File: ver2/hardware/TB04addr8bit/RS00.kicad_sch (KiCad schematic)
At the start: 34 parts, among them IC201 74HC161N, IC202 74HC161N, IC203 74HC161N, IC204 74HC161N, U201 74LS253, U202 74LS253, U203 74LS253, U204 74LS253

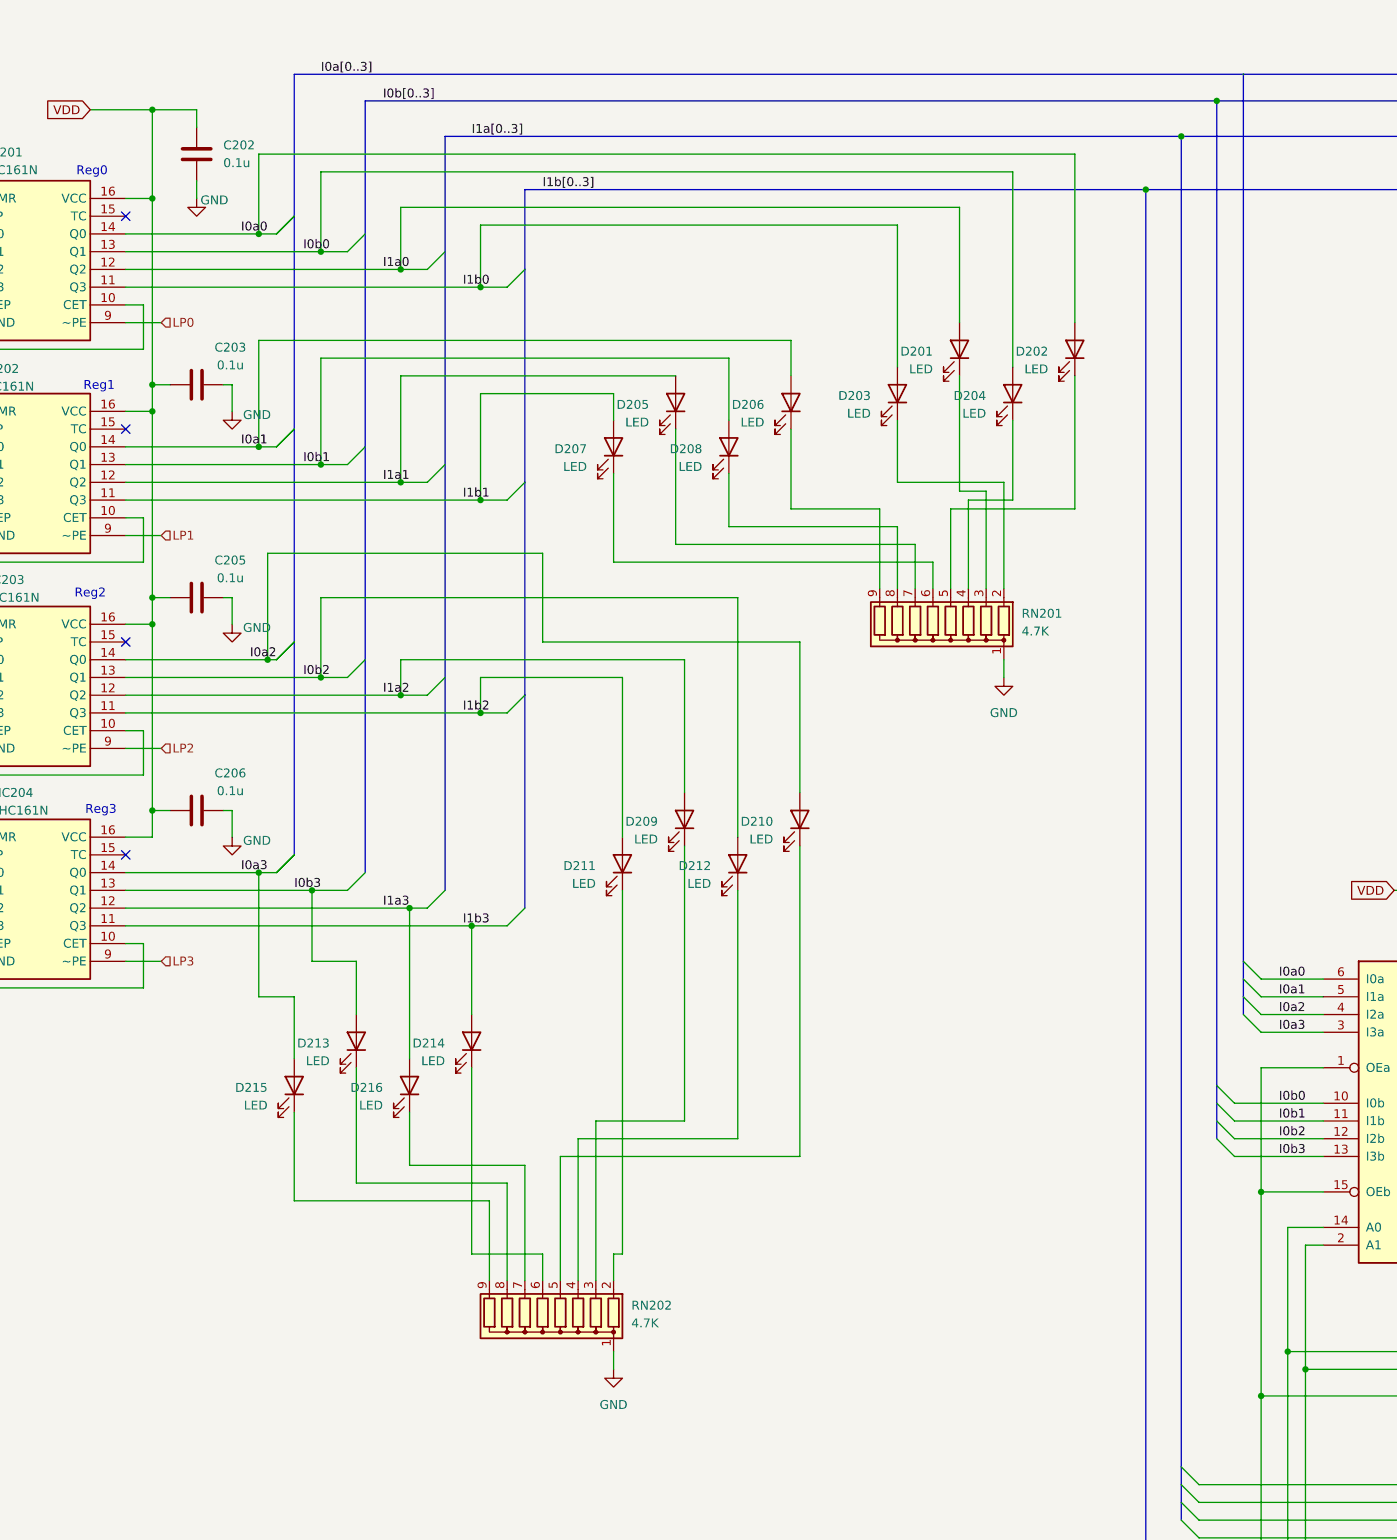
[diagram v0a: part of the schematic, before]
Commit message: ver2: 表示器を2x5コネクタ方式に変更し外付け7segIFで見せる構成に
本体のレジスタLED等を廃止し、7segIF互換の2x5コネクタ21個で外に出す方式へ。
InterFaceシートを新設しOPC/OPR0-11・MD・PC_Qを追加、R0-7とalu_codeも
コネクタ化。SP0-2のLEDを追加。既存部品のネット変更は0件で巻き添えなし。

あわせて命令ROM(U604)にバンク切替スイッチSW601(SW_Coded_SH-7050)を追加し、
A8-A11で256バイト×16バンクを選べるようにした。

要対応: A8-A11にプルダウン(10K)が無く、未選択の接点が開放で浮く。

Co-Authored-By: Claude Opus 5 <noreply@anthropic.com>
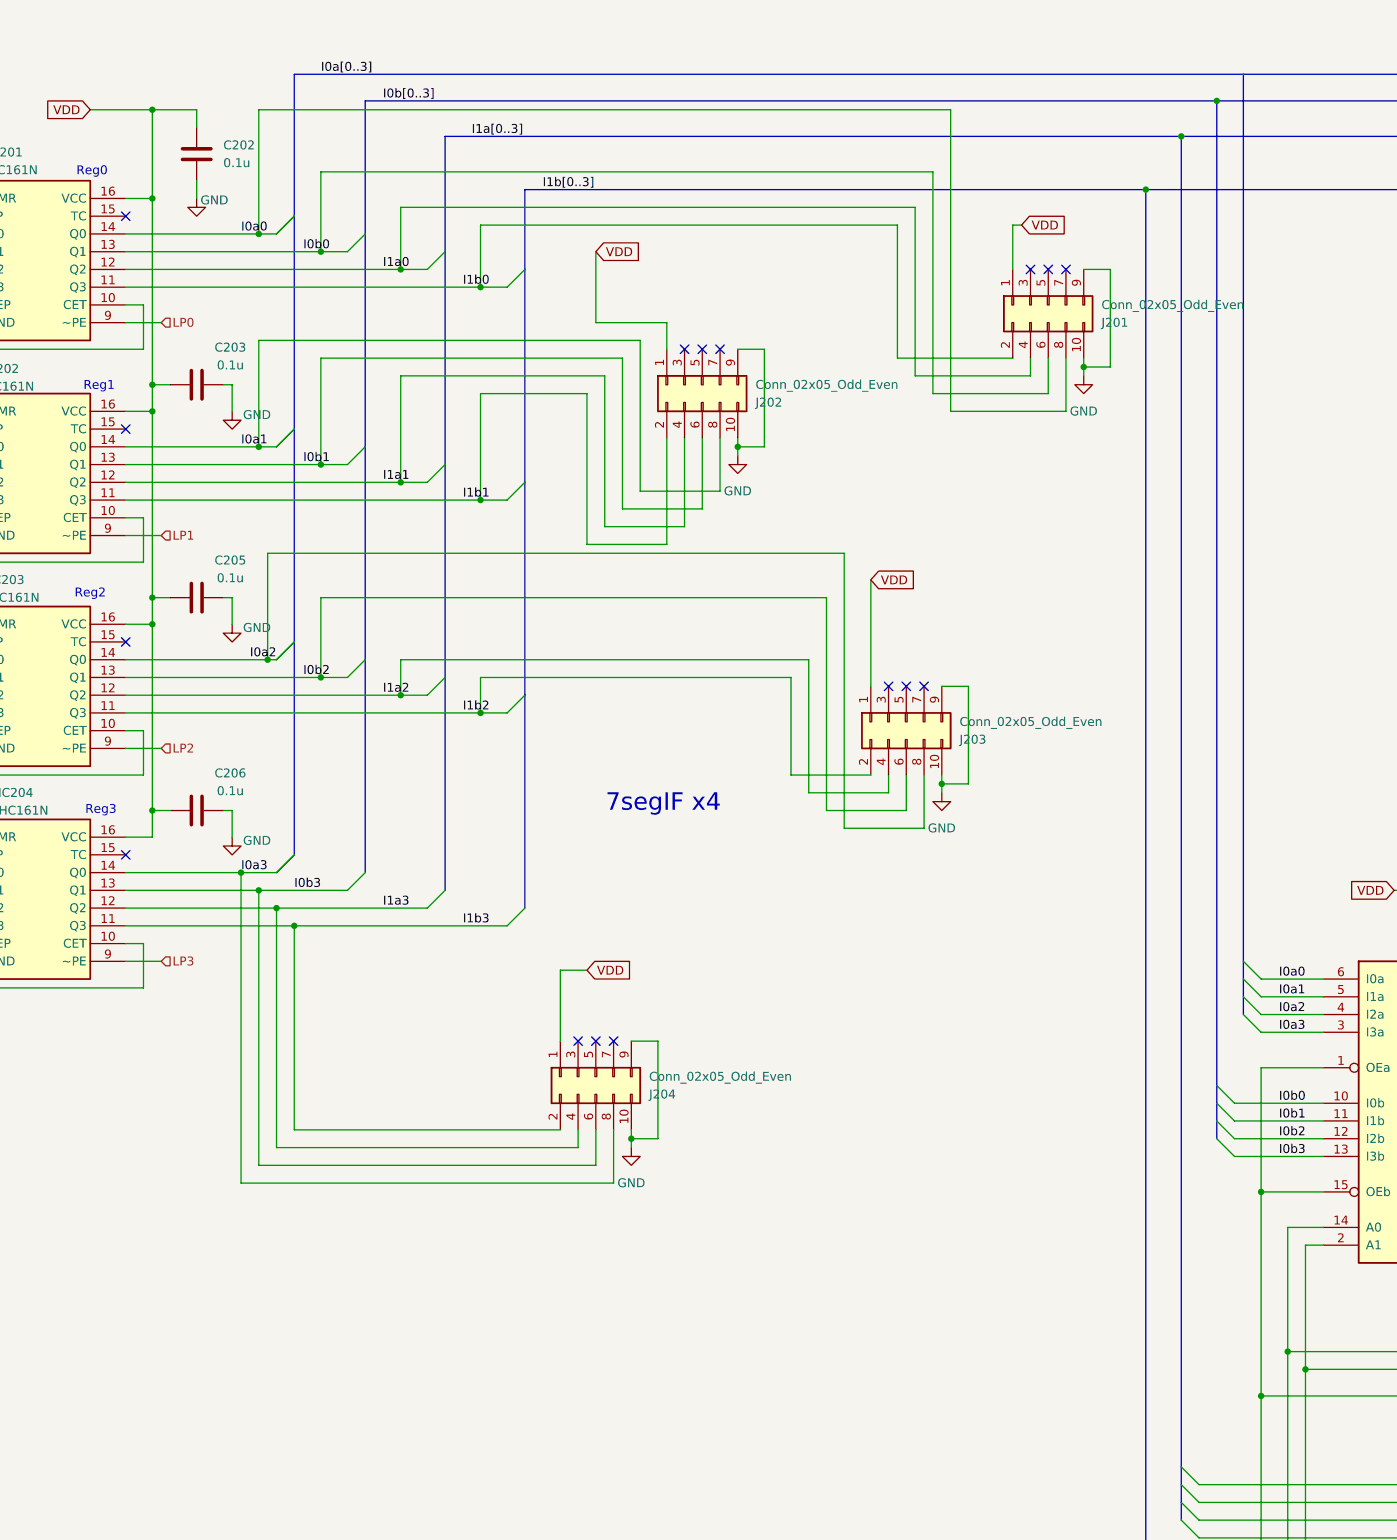
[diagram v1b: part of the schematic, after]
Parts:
- removed D201, D202, D203, D204, D205, D206, D207, D208, D209, D210, D211, D212, D213, D214, D215, D216: LED, LED_THT:LED_D3.0mm_Clear, symbol Device:LED
- removed RN201, RN202: 4.7K, Resistor_THT:R_Array_SIP9, symbol Device:R_Network08
- added J201, J202, J203, J204: Conn_02x05_Odd_Even, symbol Connector_Generic:Conn_02x05_Odd_Even
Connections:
- net GND: now also J201.10 (Pin_10), J201.9 (Pin_9), J202.10 (Pin_10), J202.9 (Pin_9), J203.10 (Pin_10), J203.9 (Pin_9), J204.10 (Pin_10), J204.9 (Pin_9)
- net I0a0: now also J201.8 (Pin_8)
- net I0a1: now also J202.8 (Pin_8)
- net I0a2: now also J203.8 (Pin_8)
- net I0a3: now also J204.8 (Pin_8)
- net I0b0: now also J201.6 (Pin_6)
- net I0b1: now also J202.6 (Pin_6)
- net I0b2: now also J203.6 (Pin_6)
- net I0b3: now also J204.6 (Pin_6)
- net I1a0: now also J201.4 (Pin_4)
- net I1a1: now also J202.4 (Pin_4)
- net I1a2: now also J203.4 (Pin_4)
- net I1a3: now also J204.4 (Pin_4)
- net I1b0: now also J201.2 (Pin_2)
- net I1b1: now also J202.2 (Pin_2)
- net I1b2: now also J203.2 (Pin_2)
- net I1b3: now also J204.2 (Pin_2)
- net VDD: now also J201.1 (Pin_1), J202.1 (Pin_1), J203.1 (Pin_1), J204.1 (Pin_1)
- no-connect marks 4 -> 16
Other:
- note added: "7segIF x4"
